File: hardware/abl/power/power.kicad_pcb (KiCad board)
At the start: 2 copper layers, 110 x 73 mm, 35 parts, among them J1 Screw_Terminal_01x03, J2 Screw_Terminal_01x03, J6 009159008603906, U2 IRM-30-5, U3 INA219AxD, U4 TMP1075D, U5 TWGMC AMS1117-3.3

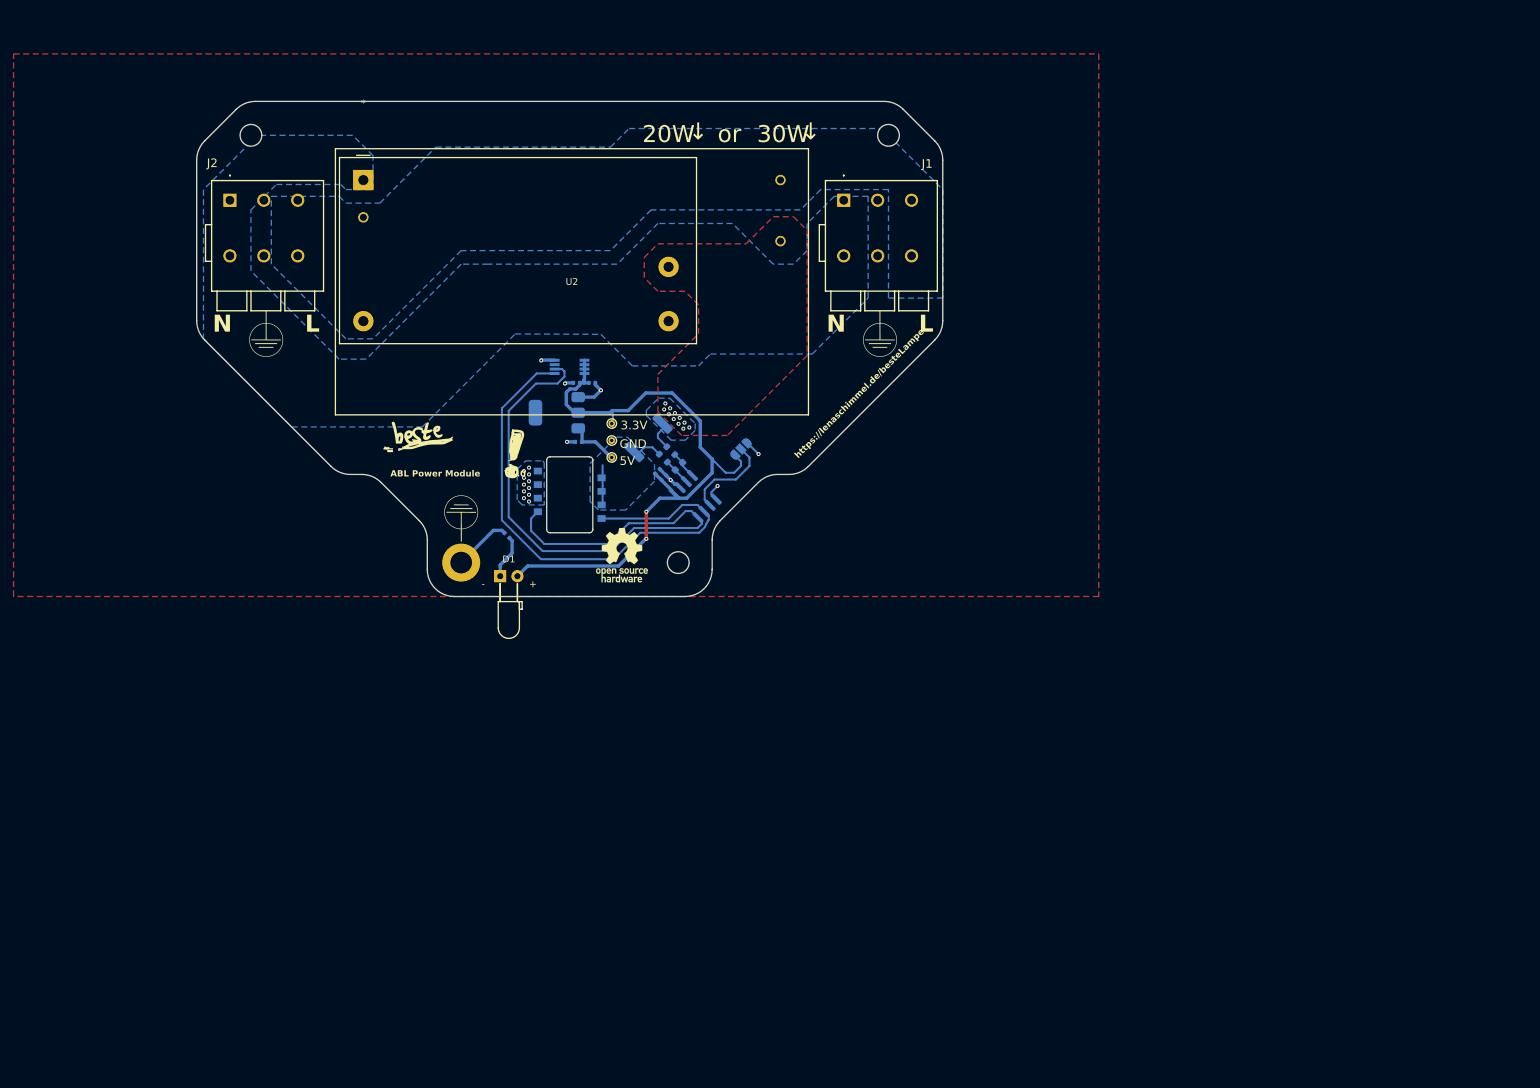
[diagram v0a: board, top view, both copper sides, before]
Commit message: Separate GND from earth protective.
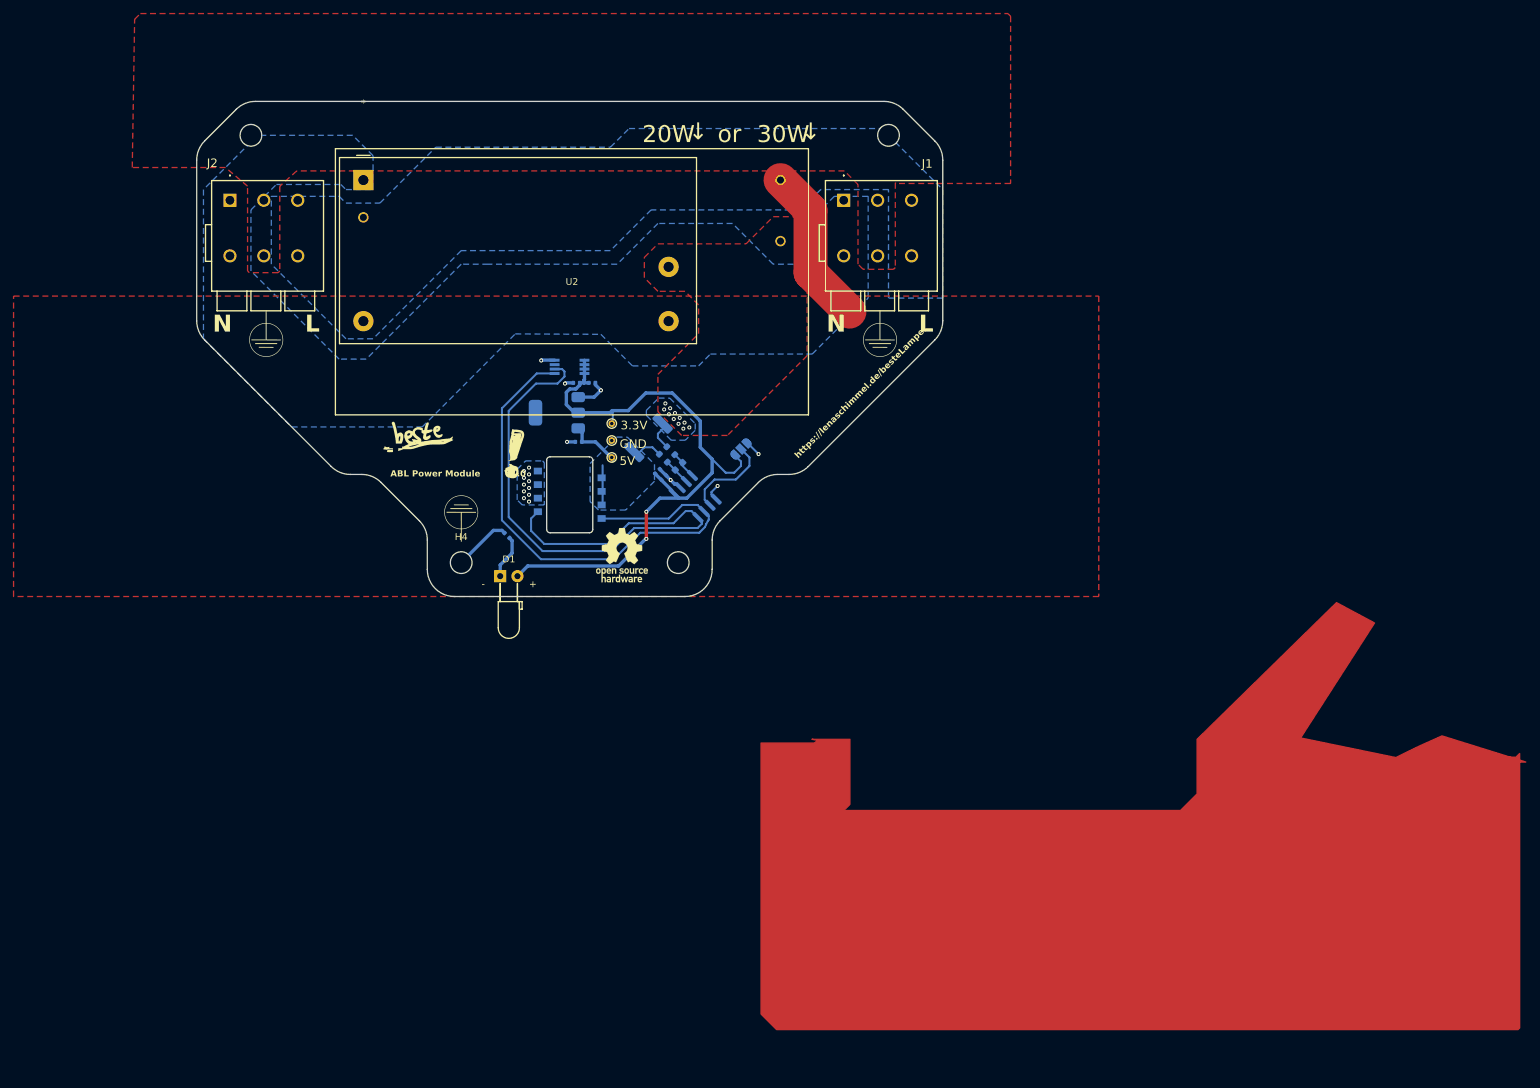
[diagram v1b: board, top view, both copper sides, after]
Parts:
- H4: value MountingHole_Pad -> MountingHole; footprint MountingHole:MountingHole_3.2mm_M3_DIN965_Pad -> MountingHole:MountingHole_3.2mm_M3_DIN965
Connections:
- net Net-(U3-SCL) renamed /SCL
- net Net-(U3-SDA) renamed /SDA
- J1 pad 3: GND -> Earth_Protective
- J1 pad 4: GND -> Earth_Protective
- J2 pad 3: GND -> Earth_Protective
- J2 pad 4: GND -> Earth_Protective
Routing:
- net GND: track 26.9 -> 50.5 mm
- added copper zone on F.Cu, net Earth_Protective

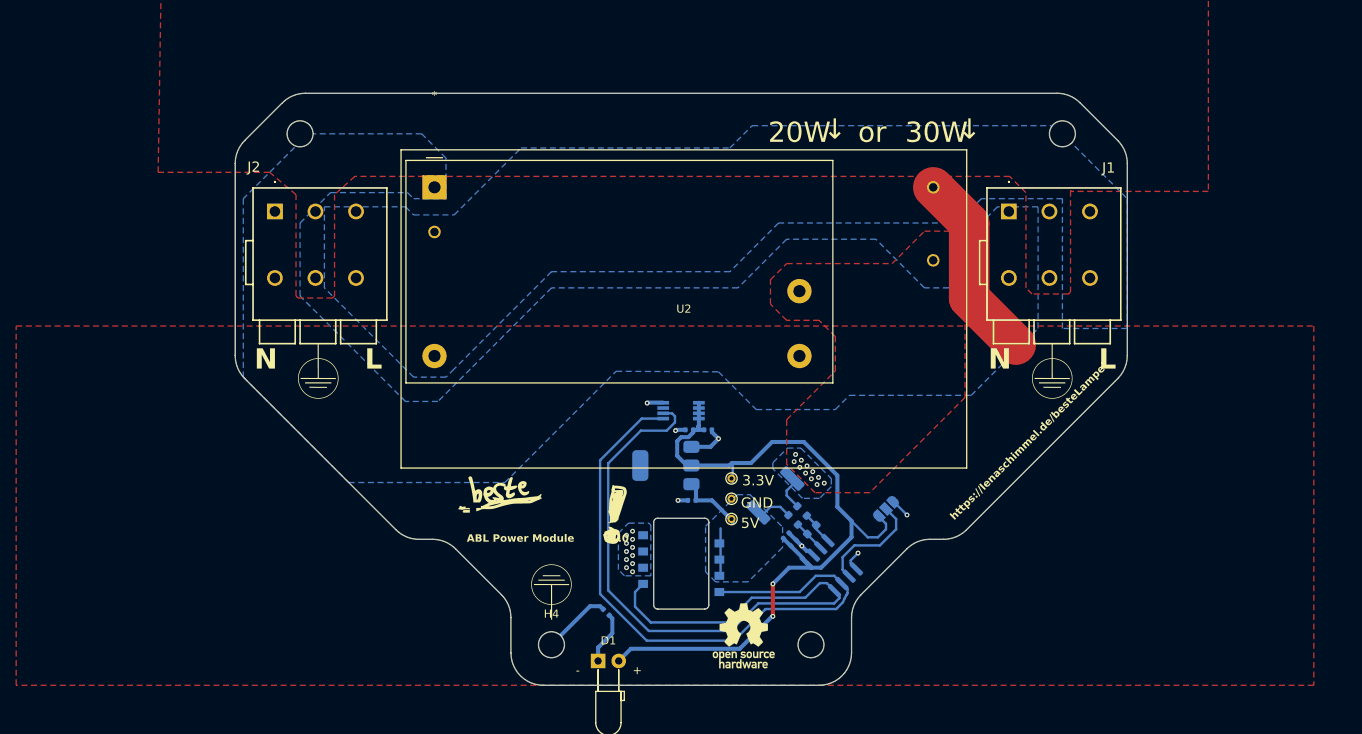
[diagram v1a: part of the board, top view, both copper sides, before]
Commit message: Enlarged PCB at the top to add protective earth connector, optimized traces and I2C return paths.
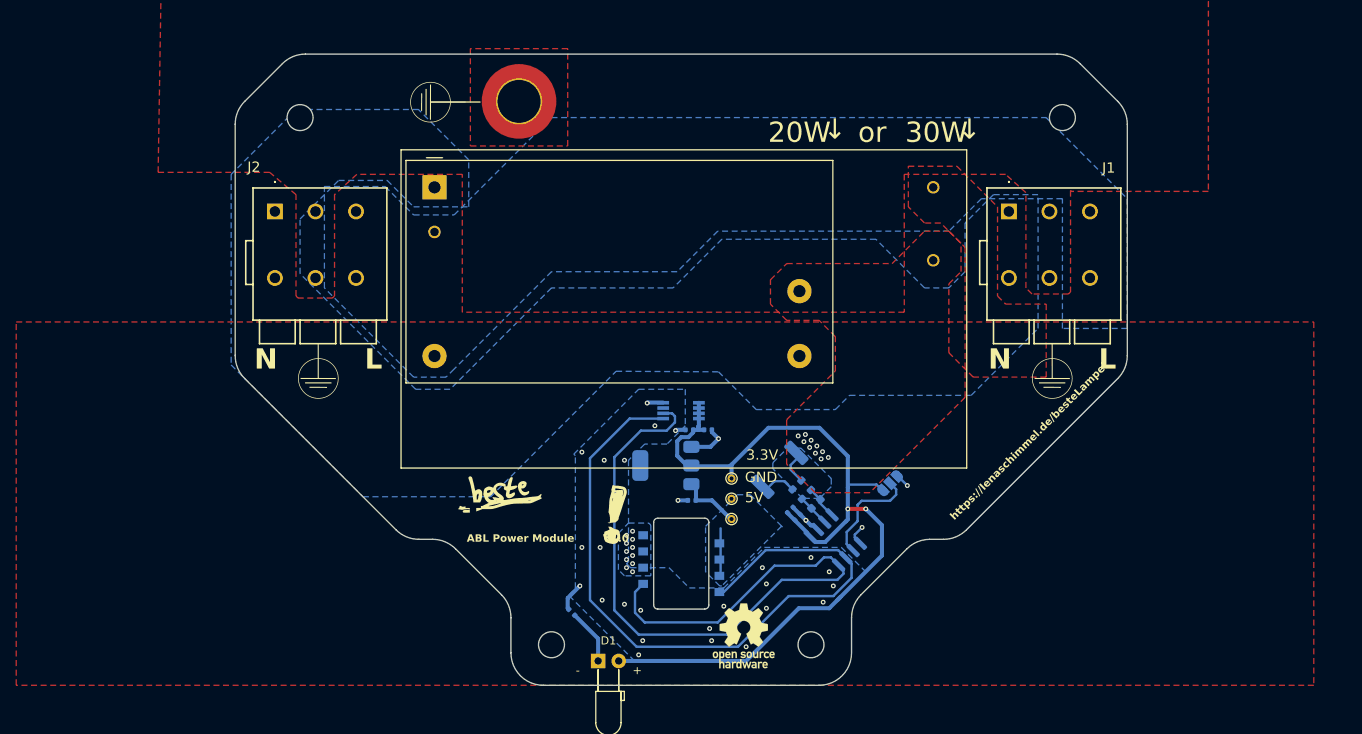
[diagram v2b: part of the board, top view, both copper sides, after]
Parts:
- added G***: LOGO, LOGO, F.Cu at (69.0, -7.90)
- added H5: MountingHole_Pad, MountingHole:MountingHole_5.3mm_M5_DIN965_Pad_TopOnly, F.Cu at (79.0, -8.00)
- G***: moved to B.Cu
- moved G*** 62.1 mm to (69.0, -8.00), turned to 90 degrees
- moved R1 4.25 mm to (85.5, 55.0)
- moved C1 3.21 mm to (112.5, 42.4)
- moved C2 3.21 mm to (113.3, 43.3)
- moved C5 3.21 mm to (115.6, 41.6)
- moved JP1 3.21 mm to (124.8, 39.1)
- moved R2 3.21 mm to (111.1, 37.4)
- moved R3 3.21 mm to (114.4, 39.3)
- moved R4 3.21 mm to (113.3, 40.4)
- moved U3 3.21 mm to (118.0, 46.1)
- moved H1 2.00 mm to (52.0, -6.00)
- moved H2 2.00 mm to (146.0, -6.00)
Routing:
- net GND: track 50.5 -> 21.2 mm, vias 18 -> 41
- net +3.3V: track 92.5 -> 105.5 mm
- net /SDA: track 79.6 -> 87.5 mm
- net /SCL: track 93.6 -> 97.7 mm
- net +5V: vias 11 -> 10
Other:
- board size 110 x 73 mm -> 110 x 77.8 mm

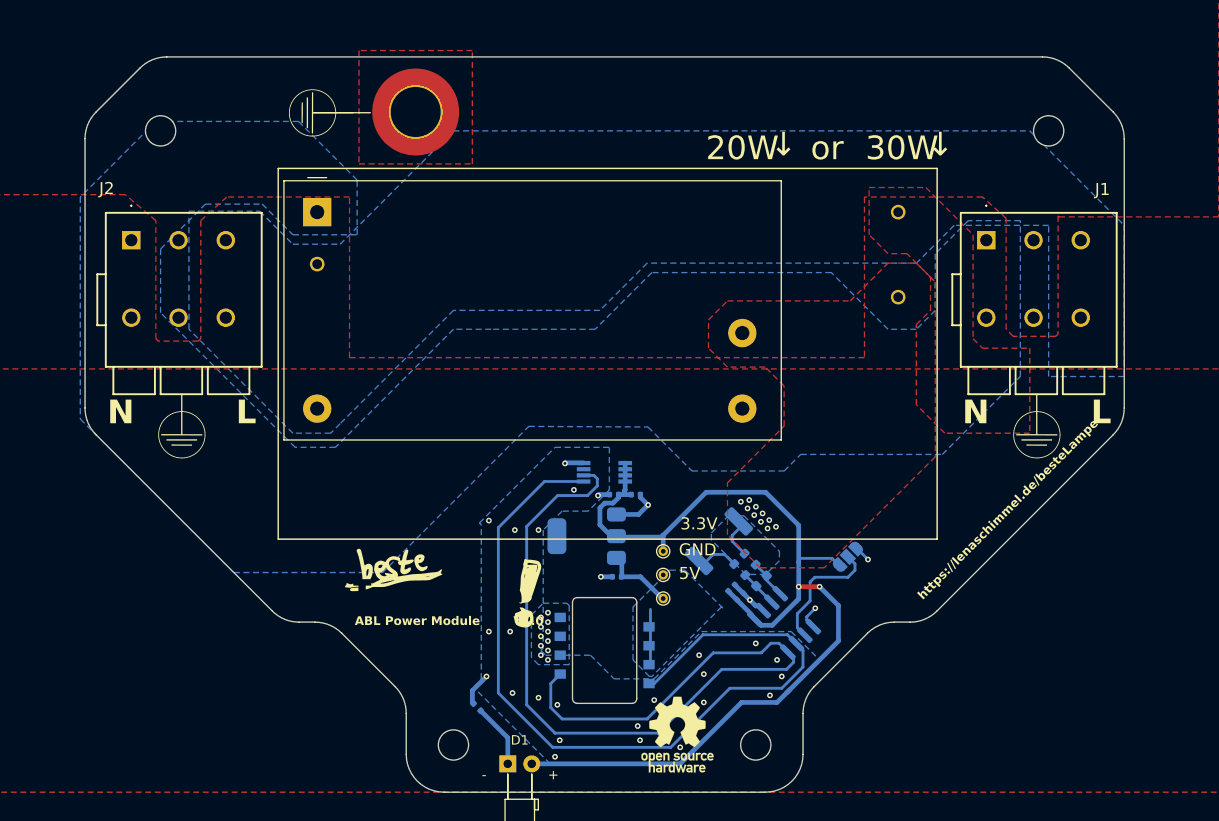
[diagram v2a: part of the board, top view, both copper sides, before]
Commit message: Revert board size, swap some mounting holes and protective earth, fix swapped N and L wires.
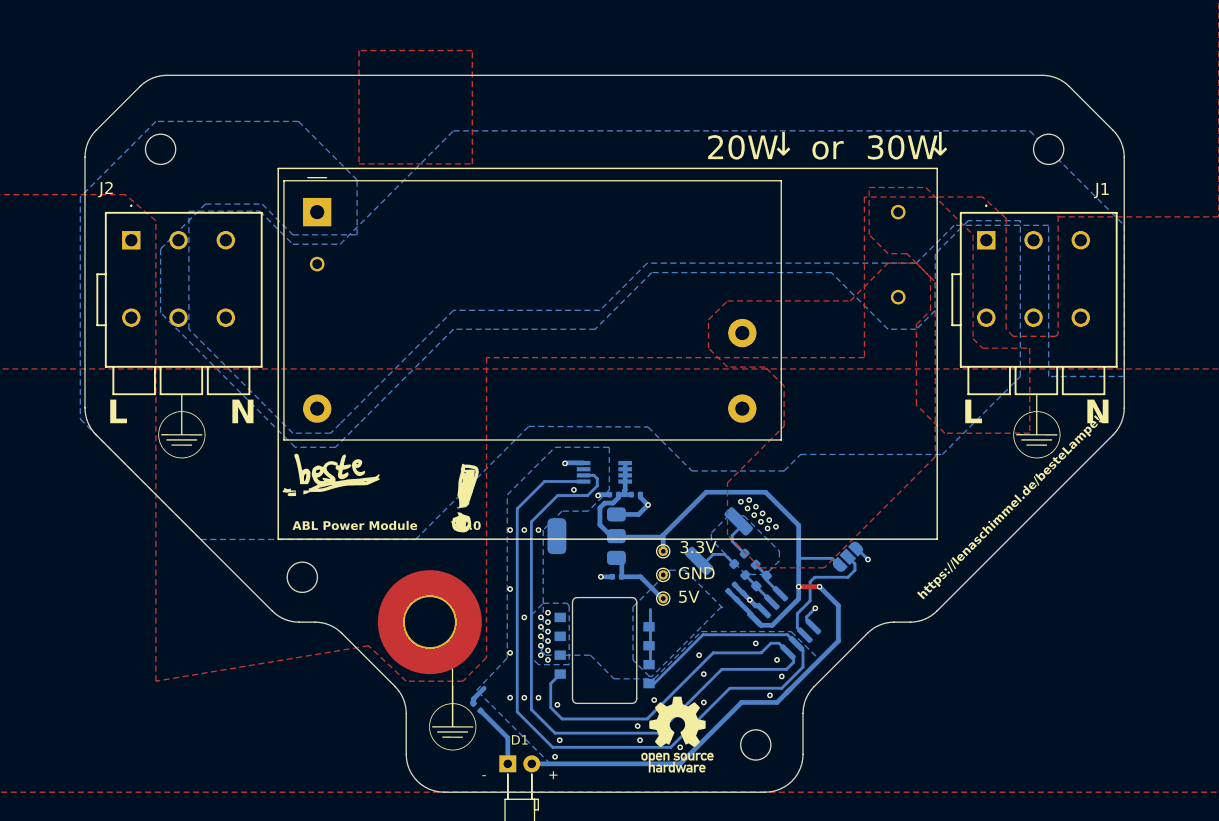
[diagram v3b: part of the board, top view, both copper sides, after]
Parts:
- moved G*** 65.6 mm to (82.8, 56.1), turned to 180 degrees
- moved G*** 65.6 mm to (82.9, 56.2), turned to 0 degrees
- moved H5 54.0 mm to (80.5, 46.0), turned to 90 degrees
- moved H4 23.9 mm to (67.0, 41.2)
- moved G*** 12.0 mm to (75.5, 32.2)
- moved H1 1.95 mm to (52.0, -4.05)
- moved H2 1.95 mm to (146.0, -4.05)
- moved REF** 1.95 mm to (101.1, -2.30)
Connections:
- J1 pad 1: /N -> /L
- J1 pad 2: /N -> /L
- J1 pad 5: /L -> /N
- J1 pad 6: /L -> /N
- J2 pad 1: /N -> /L
- J2 pad 2: /N -> /L
- J2 pad 5: /L -> /N
- J2 pad 6: /L -> /N
- PS1 pad 1: /N -> /L
- PS1 pad 2: /L -> /N
- U2 pad 1: /N -> /L
- U2 pad 2: /L -> /N
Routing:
- net /SDA: track 87.5 -> 85.8 mm
- net GND: track 21.2 -> 20.0 mm, vias 41 -> 42
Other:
- board size 110 x 77.8 mm -> 110 x 75.9 mm

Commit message: Many small optimizations and cleanups.
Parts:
- added R5: 0R, Resistor_SMD:R_0805_2012Metric, F.Cu at (90.2, 40.5)
- added REF**: Symbol_HighVoltage_Triangle_6x6mm_Copper, Symbol:Symbol_HighVoltage_Triangle_6x6mm_Copper, B.Cu at (140.5, 0.00)
- moved G*** 40.8 mm to (114.4, 44.6)
- moved REF** 36.8 mm to (68.5, 14.8)
- moved TP3 25.9 mm to (131.0, 39.0)
- moved TP1 23.9 mm to (129.0, 41.0)
- moved TP2 22.3 mm to (127.0, 43.0)
- moved G*** 8.00 mm to (89.2, 51.2)
- moved R1 6.37 mm to (90.1, 59.4), turned to 90 degrees
- moved D1 3.54 mm to (92.2, 61.8)
- moved REF** 0.42 mm to (107.0, 58.2)
- renumbered C6 to C1, C3 to C2, C4 to C3, C2 to C4, C1 to C5, C5 to C6, J6 to J3, U2 to PS2, U5 to U1, U4 to U2
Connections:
- TP1 pad 1: /5VMSR -> +5V
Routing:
- net +5V: track 3.36 -> 13.9 mm, vias 10 -> 11
- net +3.3V: track 105.5 -> 110.6 mm, vias 2 -> 0
- net Earth_Protective: track 0.00 -> 4.27 mm
- net Net-(D1-K): track 7.59 -> 3.46 mm
- net Net-(JP1-C): track 13.5 -> 12.6 mm
- net /5VMSR: track 17.2 -> 17.9 mm
- net GND: vias 42 -> 44
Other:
- board text added: "Power LED"
